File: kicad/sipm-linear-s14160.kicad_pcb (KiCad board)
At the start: 4 copper layers, 90.8 x 68.9 mm, 209 parts, among them J1 SSQ-103-01-G-D, J10 Conn_Coaxial, J11 Conn_Coaxial, J12 Conn_Coaxial, J13 Conn_Coaxial, J14 Conn_Coaxial, J15 Conn_Coaxial, J16 Conn_Coaxial, J17 Conn_Coaxial, J18 SSQ-103-01-G-D, J2 Conn_Coaxial, J3 Conn_Coaxial, J4 Conn_Coaxial, J5 Conn_Coaxial, J6 Conn_Coaxial, J7 Conn_Coaxial, J8 Conn_Coaxial, J9 Conn_Coaxial, U1 OPA847IDBVT, U10 OPA847IDBVT, U11 OPA847IDBVT, U12 OPA847IDBVT, U13 OPA847IDBVT, U14 OPA847IDBVT, U15 OPA847IDBVT, U16 OPA847IDBVT, U17 OPA847IDBVT, U2 S15643, U3 OPA847IDBVT, U4 OPA847IDBVT, U5 OPA847IDBVT, U6 OPA847IDBVT, U7 OPA847IDBVT, U8 OPA847IDBVT, U9 OPA847IDBVT

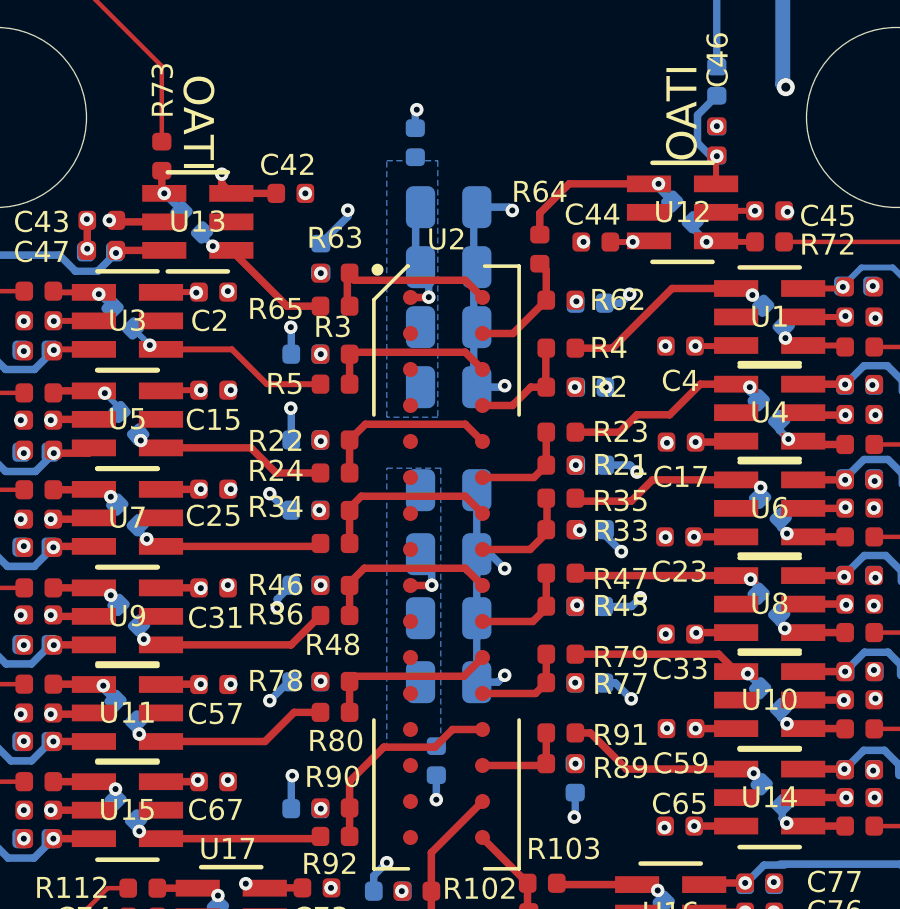
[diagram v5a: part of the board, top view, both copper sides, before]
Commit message: Change decoupling to 1206
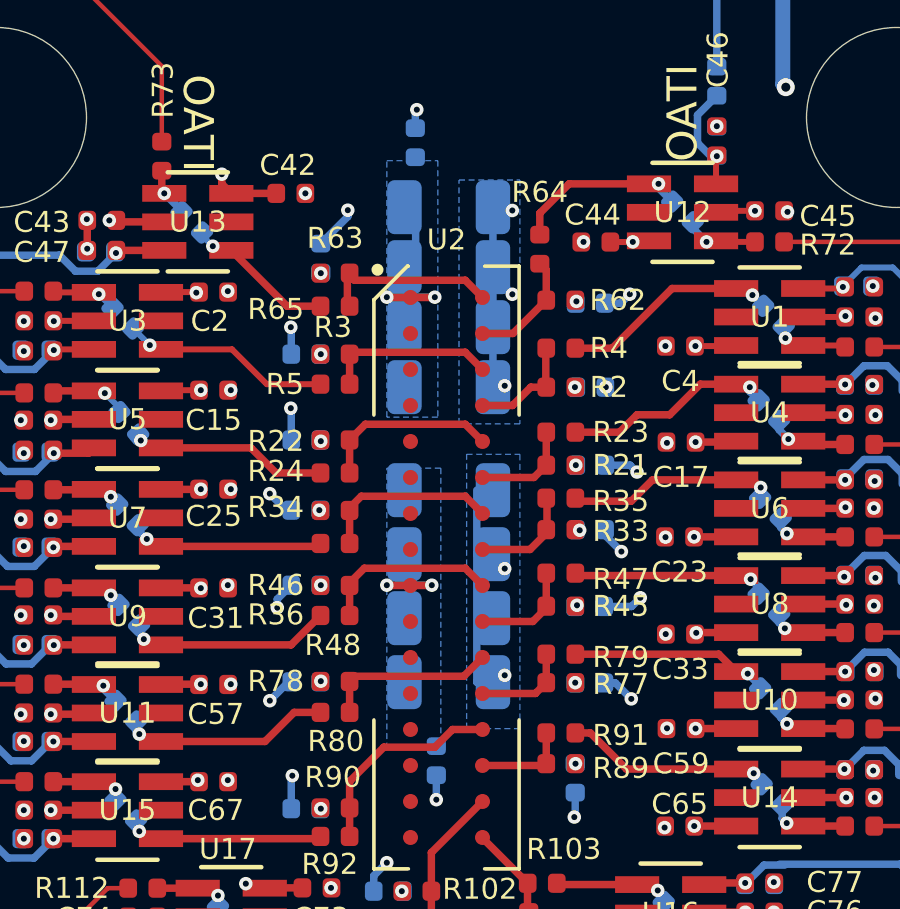
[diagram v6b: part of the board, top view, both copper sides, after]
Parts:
- C1, C10, C11, C12, C14, C39, C40, C41: footprint Capacitor_SMD:C_0805_2012Metric -> Capacitor_SMD:C_1206_3216Metric
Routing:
- net Net-(C14-Pad1): track 1.90 -> 4.87 mm, vias 1 -> 2
- net GND: track 33.5 -> 31.4 mm, vias 69 -> 70
- net Net-(C1-Pad1): track 3.18 -> 5.21 mm, vias 1 -> 2
- added copper zone on B.Cu, net GND
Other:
- board text added: "+5V USB"
- board text added: "SIPM Linear S14420 Custom Array V1.1"
- board text removed: "SIPM Linear S14420 Custom Array V1.0"

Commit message: Fix track under drill hole
Pretty sure JLCPCB quietly fixed this for us on the initial design.
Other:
- board text added: "+5"
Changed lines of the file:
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@@
     (effects (font (size 1 1) (thickness 0.11)) (justify mirror))
+  )
+  (gr_text "+5" (at 187.3 136.9) (layer "B.SilkS")
+    (effects (font (size 0.508 0.508) (thickness 0.0762)) (justify mirror))
   )
   (gr_text "CH10" (at 141.6 131.8) (layer "B.SilkS")
@@
     (effects (font (size 1.5 1.5) (thickness 0.3)) (justify mirror))
   )
+  (gr_text "+5" (at 181.1 71.7) (layer "B.SilkS")
+    (effects (font (size 0.508 0.508) (thickness 0.0762)) (justify mirror))
+  )
   (gr_text "CH5" (at 227 86.3) (layer "B.SilkS")

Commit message: Check in more changes
Forgot to hit save before last commits.
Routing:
- net Net-(J17-In): track 25.5 -> 28.7 mm
